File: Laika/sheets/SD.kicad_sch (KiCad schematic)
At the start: 18 parts, among them J5 Micro_SD_Card, Q3 MMBT5551, Q4 Si2301CDS

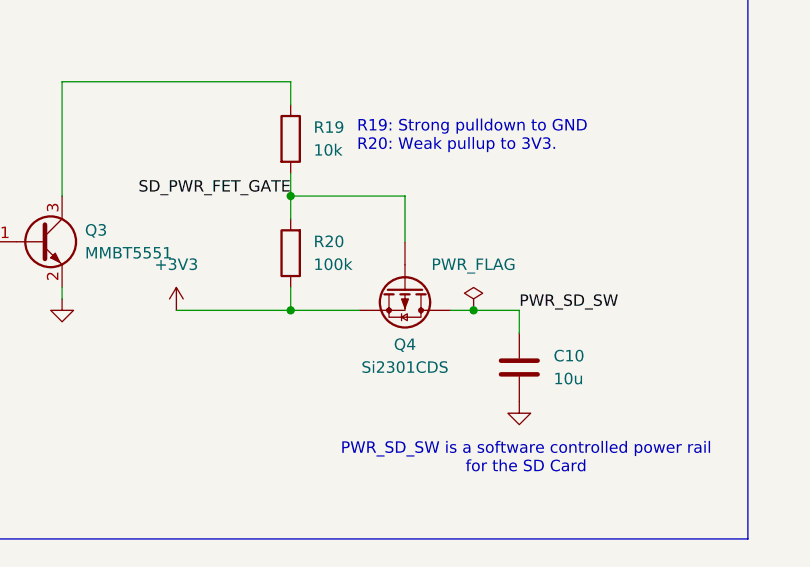
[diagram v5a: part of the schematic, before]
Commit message: Replace generic PMOS with symbol for SI203xxxx
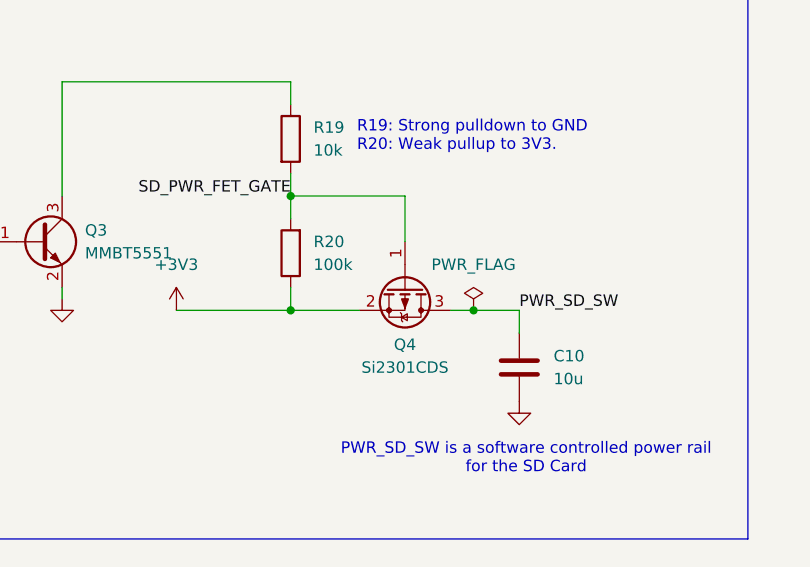
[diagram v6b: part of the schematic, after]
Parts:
- Q4: footprint Package_TO_SOT_SMD:SOT-23-3 -> Package_TO_SOT_SMD:SOT-23; symbol Device:Q_PMOS -> Transistor_FET:Si2319CDS
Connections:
- net +3V3: now also Q4.2 (S); no longer Q4.S
- net PWR_SD_SW: now also Q4.3 (D); no longer Q4.D
- net SD_PWR_FET_GATE: now also Q4.1 (G); no longer Q4.G
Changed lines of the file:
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@@
 	)
 	(symbol
-		(lib_id "Device:Q_PMOS")
+		(lib_id "Transistor_FET:Si2319CDS")
 		(at 101.6 86.36 270)
 		(unit 1)
@@
 			)
 		)
-		(property "Footprint" "Package_TO_SOT_SMD:SOT-23-3"
-			(at 104.14 91.44 0)
+		(property "Footprint" "Package_TO_SOT_SMD:SOT-23"
+			(at 99.695 91.44 0)
+			(effects
+				(font
+					(size 1.27 1.27)
+					(italic yes)
+				)
+				(justify left)
+				(hide yes)
+			)
+		)
+		(property "Datasheet" "http://www.vishay.com/docs/66709/si2319cd.pdf"
+			(at 97.79 91.44 0)
 			(effects
 				(font
 					(size 1.27 1.27)
 				)
+				(justify left)
 				(hide yes)
 			)
 		)
-		(property "Datasheet" "https://www.vishay.com/docs/68741/si2301cd.pdf"
-			(at 101.6 86.36 0)
-			(effects
-				(font
-					(size 1.27 1.27)
-				)
-				(hide yes)
-			)
-		)
-		(property "Description" "P-MOSFET transistor"
+		(property "Description" "-4.4A Id, -40V Vds, P-Channel MOSFET, SOT-23"
 			(at 101.6 86.36 0)
 			(effects
@@
 			)
 		)
-		(pin "D"
+		(pin "2"
 		)
-		(pin "G"
+		(pin "1"
 		)
-		(pin "S"
+		(pin "3"
 		)
 		(instances

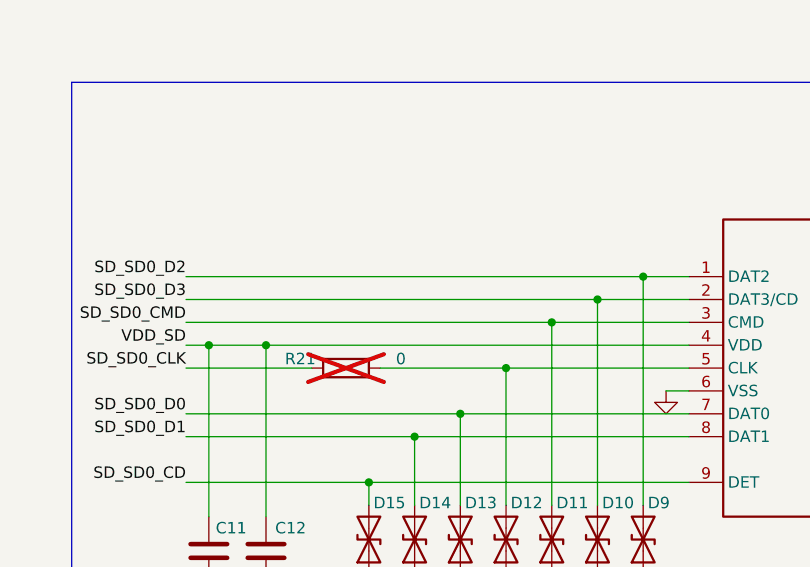
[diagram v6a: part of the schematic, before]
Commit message: Remove external GPS module for spacing constraints
Removed the Ublox GPS module and instead have just a breakout pin
header. While the module technically fit, the amount of free space
around it to follow proper design guidelines left alot of unused space.
To priotize density, GPS design guideslines, and board size, the GPS
will be external.

Signed-off-by: Aeybel Varghese <aeybelvarghese@gmail.com>
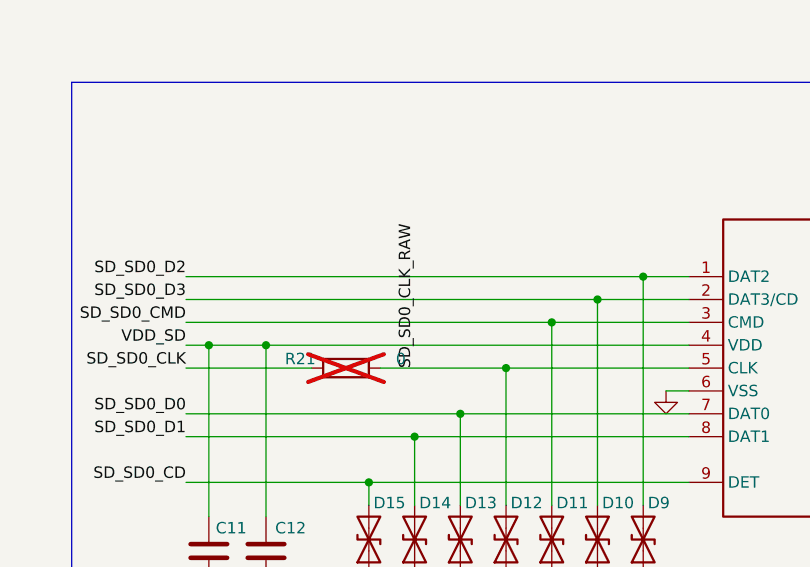
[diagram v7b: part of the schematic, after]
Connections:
- net SD_SD0_CLK_RAW: now reaches D12.2 (A2), J5.5 (CLK), R21.2
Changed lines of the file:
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@@
+		)
+	)
+	(label "SD_SD0_CLK_RAW"
+		(at 190.5 82.55 90)
+		(effects
+			(font
+				(size 1.27 1.27)
+			)
+			(justify left bottom)
 		)
 	)
